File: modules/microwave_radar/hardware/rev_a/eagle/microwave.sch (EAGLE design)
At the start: 55 parts, among them J1 MODULE_GENERIC, J2 TC2030-JLINK-L, U1 SAM4LC8AA, U2 TLV62130, U3 MSGEQ7, U4 HB100

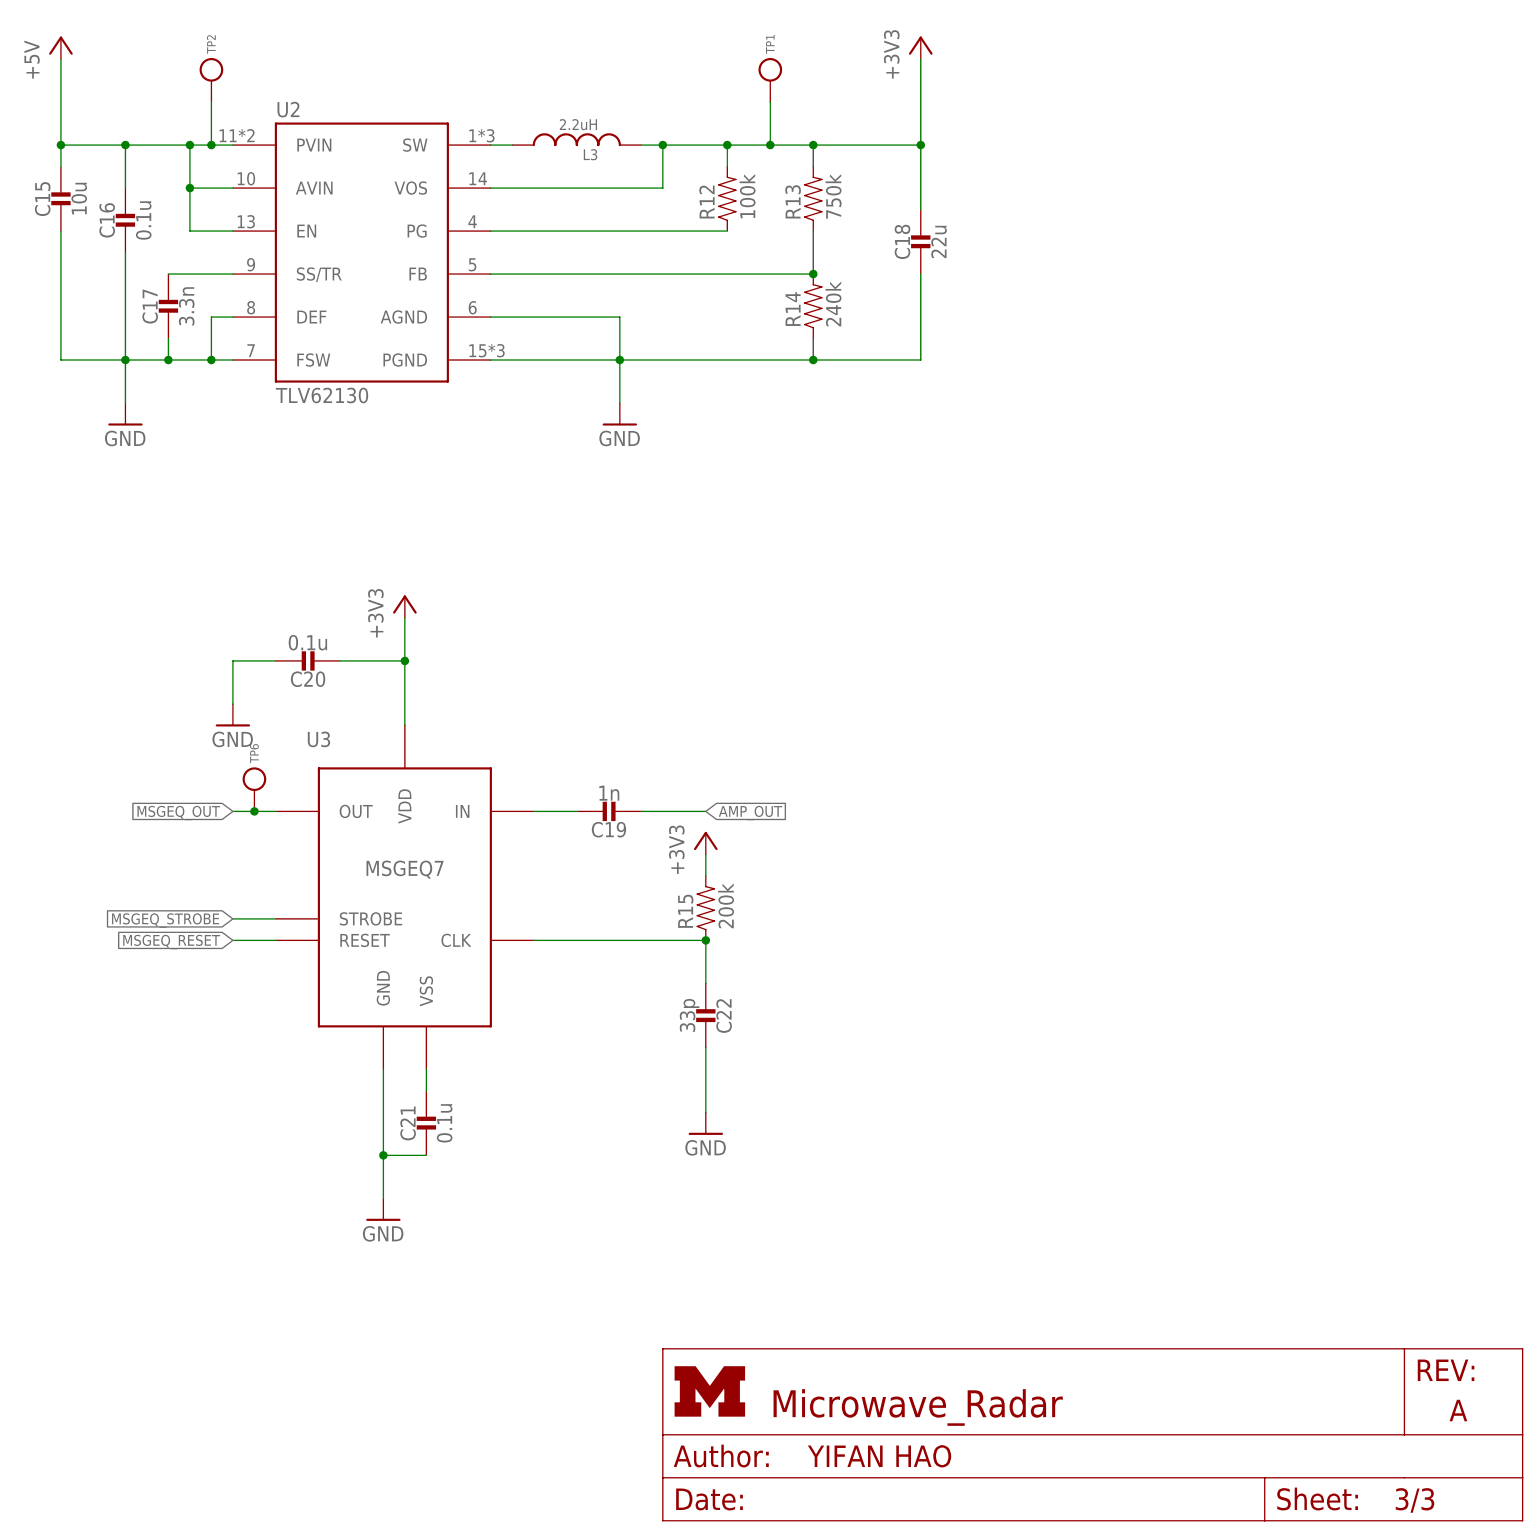
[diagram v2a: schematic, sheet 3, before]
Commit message: Fix test point and trace on the sides
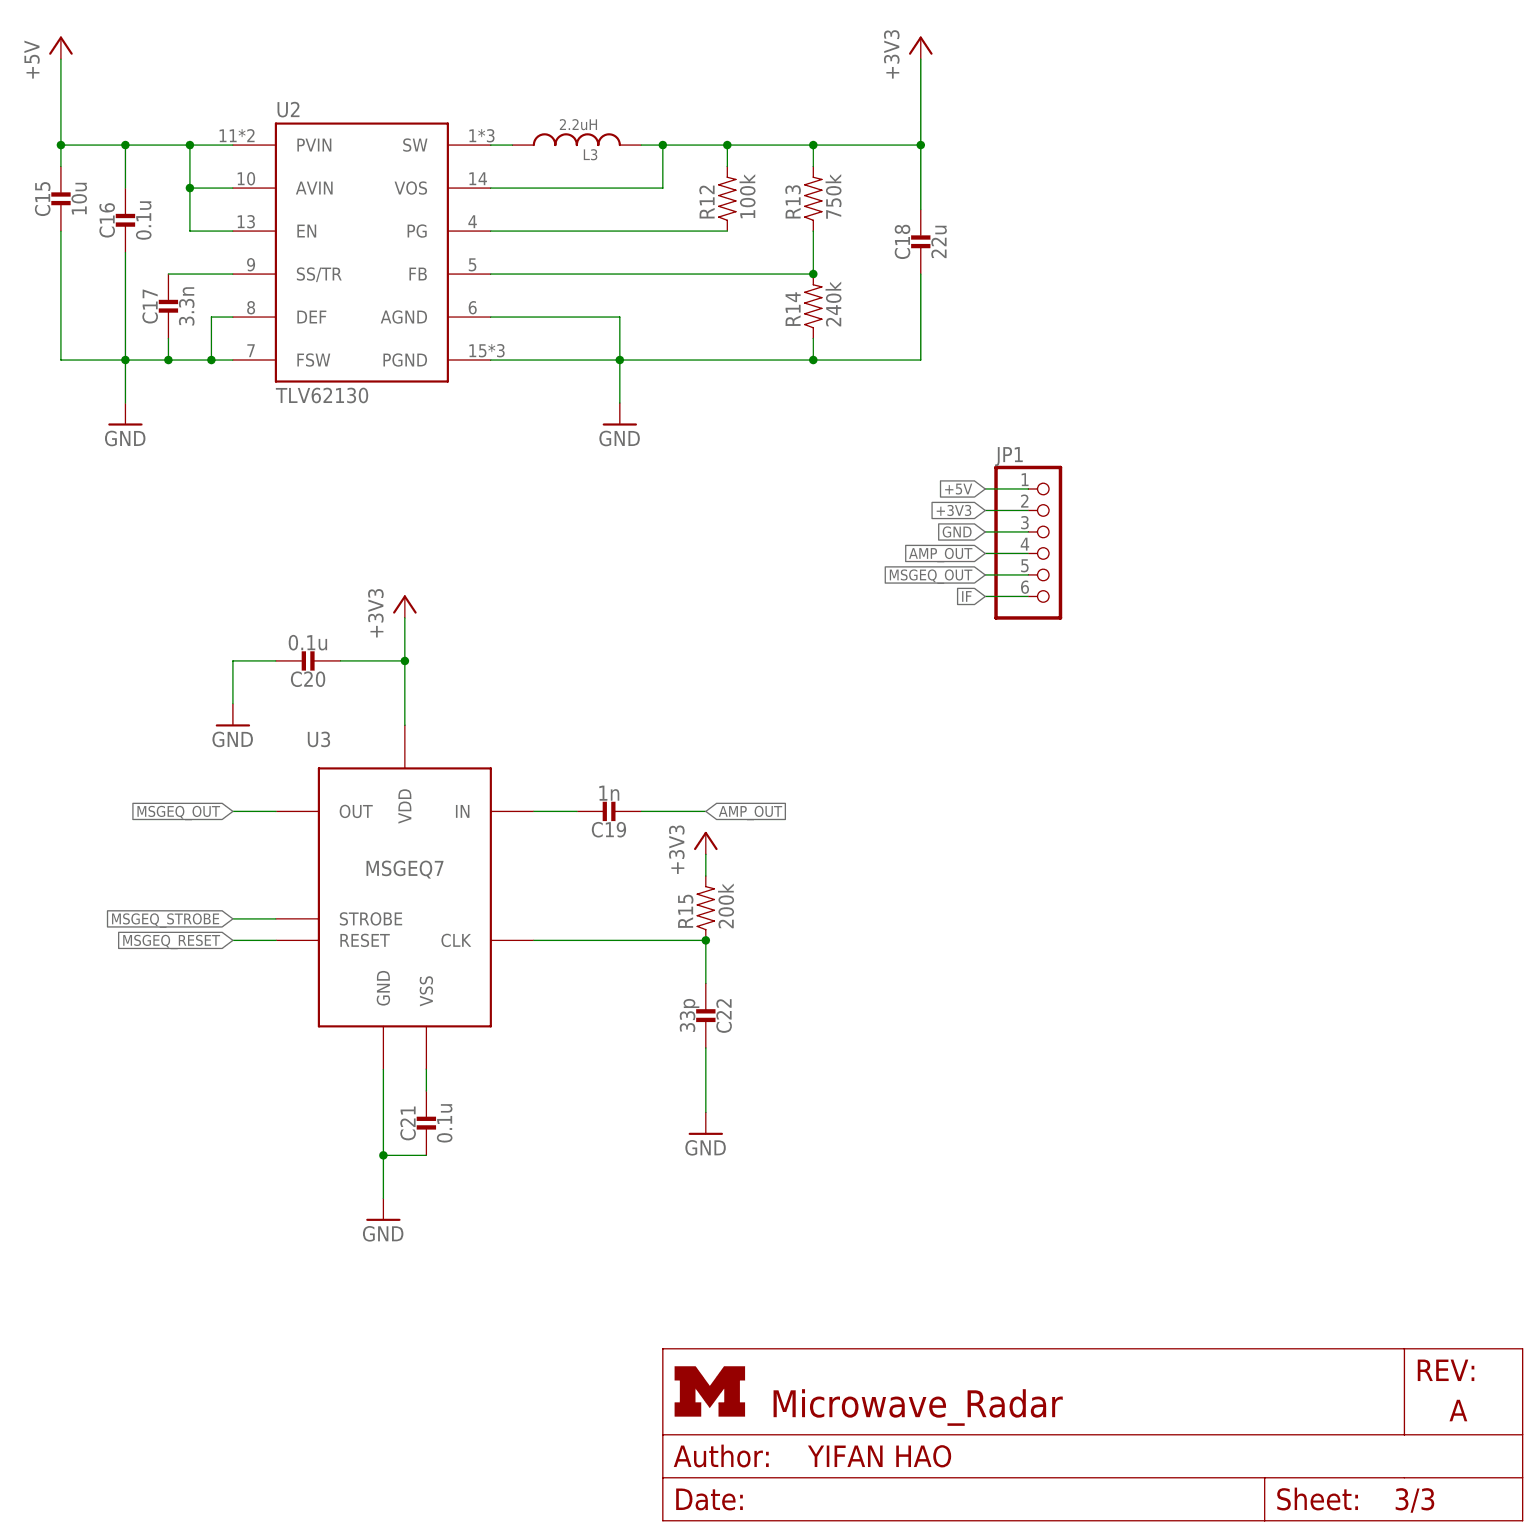
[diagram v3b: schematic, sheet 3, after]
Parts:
- removed TP1, TP2, TP3, TP4, TP5, TP6: TEST_POINT_0.040IN, headers:TEST_POINT_0.040IN
- removed U$1: OP284E_SEPARATE, microwave_radar:OP284E_SEPARATE
- added JP1: (no value), pinhead:PINHD-1X6
- added U5: OP284E_SEPARATE, microwave_radar:OP284E_SEPARATE
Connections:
- net +3V3: now also JP1.2, U5G$2.VCC; no longer TP1.TESTPOINT, U$1G$2.VCC
- net +5V: now also JP1.1; no longer TP2.TESTPOINT
- net AMP_OUT: now also JP1.4, U5_B.OUT_B; no longer TP4.TESTPOINT, U$1G$1.OUT_B
- net GND: now also JP1.3, U5G$2.GND; no longer TP5.TESTPOINT, U$1G$2.GND
- net IF: now also JP1.6; no longer TP3.TESTPOINT
- net MSGEQ_OUT: now also JP1.5; no longer TP6.TESTPOINT
- net N$1: now also U5_B.+IN_B; no longer U$1G$1.+IN_B
- net N$12: now also U5_A.-IN_A; no longer U$1OP284E_A.-IN_A
- net N$17: now also U5_A.OUT_A; no longer U$1OP284E_A.OUT_A
- net N$19: now also U5_B.-IN_B; no longer U$1G$1.-IN_B
- net N$9: now also U5_A.+IN_A; no longer U$1OP284E_A.+IN_A

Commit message: Add attributes for several parts
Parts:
- R3, R4, R5, R8: DIGIKEY (none) -> 1276-3432-1-ND
- R6: DIGIKEY (none) -> 1276-3431-1-ND
- U5: DIGIKEY (none) -> OP284ESZ-ND
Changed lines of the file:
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@@
 <part name="GND1" library="umich" deviceset="GND" device=""/>
 <part name="R2" library="passives" deviceset="RESISTOR" device="0402_RES" value="330k"/>
-<part name="R3" library="passives" deviceset="RESISTOR" device="0402_RES" value="100k"/>
-<part name="R4" library="passives" deviceset="RESISTOR" device="0402_RES" value="100k"/>
+<part name="R3" library="passives" deviceset="RESISTOR" device="0402_RES" value="100k">
+<attribute name="DIGIKEY" value="1276-3432-1-ND"/>
+</part>
+<part name="R4" library="passives" deviceset="RESISTOR" device="0402_RES" value="100k">
+<attribute name="DIGIKEY" value="1276-3432-1-ND"/>
+</part>
 <part name="C2" library="passives" deviceset="CAPACITOR" device="0402_CAP" value="100u"/>
 <part name="GND2" library="umich" deviceset="GND" device=""/>
-<part name="R5" library="passives" deviceset="RESISTOR" device="0402_RES" value="100k"/>
-<part name="R6" library="passives" deviceset="RESISTOR" device="0402_RES" value="10k"/>
+<part name="R5" library="passives" deviceset="RESISTOR" device="0402_RES" value="100k">
+<attribute name="DIGIKEY" value="1276-3432-1-ND"/>
+</part>
+<part name="R6" library="passives" deviceset="RESISTOR" device="0402_RES" value="10k">
+<attribute name="DIGIKEY" value="1276-3431-1-ND"/>
+</part>
 <part name="C3" library="passives" deviceset="CAPACITOR" device="0402_CAP" value="4.7u"/>
 <part name="C4" library="passives" deviceset="CAPACITOR" device="0402_CAP" value="2.2n"/>
@@
 <part name="R7" library="passives" deviceset="RESISTOR" device="0402_RES" value="8.2k"/>
 <part name="C7" library="passives" deviceset="CAPACITOR" device="0402_CAP" value="2.2n"/>
-<part name="R8" library="passives" deviceset="RESISTOR" device="0402_RES" value="100k"/>
+<part name="R8" library="passives" deviceset="RESISTOR" device="0402_RES" value="100k">
+<attribute name="DIGIKEY" value="1276-3432-1-ND"/>
+</part>
 <part name="R11" library="passives" deviceset="RESISTOR" device="0402_RES" value="10k">
 <attribute name="DIGIKEY" value="1276-3431-1-ND"/>
@@
 <part name="GND7" library="umich" deviceset="GND" device=""/>
 <part name="U4" library="microwave_radar" deviceset="HB100" device=""/>
-<part name="U5" library="microwave_radar" deviceset="OP284E_SEPARATE" device=""/>
+<part name="U5" library="microwave_radar" deviceset="OP284E_SEPARATE" device="">
+<attribute name="DIGIKEY" value="OP284ESZ-ND"/>
+</part>
 <part name="JP1" library="pinhead" deviceset="PINHD-1X6" device=""/>
 </parts>
@@
 <instance part="GND1" gate="1" x="17.78" y="25.4"/>
 <instance part="R2" gate="G$1" x="38.1" y="58.42" rot="R90"/>
-<instance part="R3" gate="G$1" x="22.86" y="73.66" rot="R90"/>
-<instance part="R4" gate="G$1" x="22.86" y="91.44" rot="R90"/>
+<instance part="R3" gate="G$1" x="22.86" y="73.66" rot="R90">
+<attribute name="DIGIKEY" x="22.86" y="73.66" size="1.778" layer="96" rot="R90" display="off"/>
+</instance>
+<instance part="R4" gate="G$1" x="22.86" y="91.44" rot="R90">
+<attribute name="DIGIKEY" x="22.86" y="91.44" size="1.778" layer="96" rot="R90" display="off"/>
+</instance>
 <instance part="C2" gate="G$1" x="5.08" y="73.66" rot="R180"/>
 <instance part="GND2" gate="1" x="22.86" y="58.42"/>
-<instance part="R5" gate="G$1" x="45.72" y="10.16" rot="R180"/>
-<instance part="R6" gate="G$1" x="33.02" y="10.16" rot="R180"/>
+<instance part="R5" gate="G$1" x="45.72" y="10.16" rot="R180">
+<attribute name="DIGIKEY" x="45.72" y="10.16" size="1.778" layer="96" rot="R180" display="off"/>
+</instance>
+<instance part="R6" gate="G$1" x="33.02" y="10.16" rot="R180">
+<attribute name="DIGIKEY" x="33.02" y="10.16" size="1.778" layer="96" rot="R180" display="off"/>
+</instance>
 <instance part="C3" gate="G$1" x="20.32" y="10.16" rot="R90"/>
 <instance part="C4" gate="G$1" x="45.72" y="-2.54" rot="R90"/>
@@
 <instance part="R7" gate="G$1" x="104.14" y="43.18" rot="R180"/>
 <instance part="C7" gate="G$1" x="127" y="25.4" rot="R90"/>
-<instance part="R8" gate="G$1" x="127" y="12.7" rot="R180"/>
+<instance part="R8" gate="G$1" x="127" y="12.7" rot="R180">
+<attribute name="DIGIKEY" x="127" y="12.7" size="1.778" layer="96" rot="R180" display="off"/>
+</instance>
 <instance part="GND6" gate="1" x="157.48" y="88.9"/>
 <instance part="+3V1" gate="G$1" x="22.86" y="109.22"/>
@@
 <instance part="GND7" gate="1" x="76.2" y="104.14"/>
 <instance part="U4" gate="G1" x="160.02" y="116.84"/>
-<instance part="U5" gate="_A" x="60.96" y="43.18"/>
+<instance part="U5" gate="_A" x="60.96" y="43.18">
+<attribute name="DIGIKEY" x="60.96" y="43.18" size="1.778" layer="96" display="off"/>
+</instance>
 <instance part="U5" gate="_B" x="119.38" y="45.72"/>
 <instance part="U5" gate="G$2" x="76.2" y="121.92"/>

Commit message: Run Pat's script
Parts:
- C1: value 4.7u -> 8pF; DIGIKEY (none) -> 490-8230-1-ND
- C10, C9: value 100n -> 0.1uF; DIGIKEY 490-10777-1-ND -> (none)
- C11, C12, C14: value 100n -> 100nF
- C13: value 100n -> 100nF; DIGIKEY 490-13252-1-ND -> 490-10777-1-ND
- C15: value 10u -> 100nF; DIGIKEY (none) -> 490-13252-1-ND
- C16: value 0.1u -> 100nF; DIGIKEY (none) -> 490-10777-1-ND
- C17: value 3.3n -> 4.7uF
- C18: value 22u -> 4.7uF
- C19: value 1n -> 4.7uF
- C2: value 100u -> 8pF; DIGIKEY (none) -> 490-8230-1-ND
- C20: value 0.1u -> 10uF
- C21: value 0.1u -> 22uF
- C22: value 33p -> 100uF
- C3: value 4.7u -> 33pF
- C4: value 2.2n -> 1nF
- C5: value 4.7u -> 2.2nF
- C6: value 8pF -> 2.2nF; DIGIKEY 490-8230-1-ND -> (none)
- C7: value 2.2n -> 3.3nF
- C8: value 8pF -> 0.1uF; DIGIKEY 490-8230-1-ND -> (none)
- L1: value 1.5k -> 2.2uH; device passives:FERRITE_BEAD0402 -> passives:INDUCTORIHL; DIGIKEY 490-5216-1-ND -> (none)
- L3: value 2.2uH -> 1.5k; device passives:INDUCTORIHL -> passives:FERRITE_BEAD0402; DIGIKEY (none) -> 490-5216-1-ND
- R1: value 12k -> 8.2k
- R11: value 10k -> 100k; DIGIKEY 1276-3431-1-ND -> (none)
- R12: value 100k -> 200k
- R13: value 750k -> 240k
- R14: value 240k -> 330k
- R15: value 200k -> 750k
- R2: value 330k -> 10k; DIGIKEY (none) -> 1276-3431-1-ND
- R3: value 100k -> 10k; DIGIKEY 1276-3432-1-ND -> 1276-3431-1-ND
- R4: value 100k -> 12k; DIGIKEY 1276-3432-1-ND -> (none)
- R6: value 10k -> 100k; DIGIKEY 1276-3431-1-ND -> 1276-3432-1-ND
- R7: value 8.2k -> 100k; DIGIKEY (none) -> 1276-3432-1-ND
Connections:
- net +3V3: now also C12.2, C13.2, C21.1, L1.2, L3.P$2, R3.2, R5.2, R6.2, R8.2; no longer C10.2, C18.1, C20.2, L1.P$2, L3.2, R10.2, R13.2, R4.2, R9.2
- net +5V: now also C20.1, C8.1; no longer C15.1, C16.1
- net AMP_OUT: now also C4.2, C6.2, R10.1; no longer C19.2, C7.2, R8.1
- net CONTROLLER_SWDCLK: now also R6.1; no longer R10.1
- net CONTROLLER_SWDIO: now also R5.1; no longer R9.1
- net CONTROLLER_XIN: now also C1.1; no longer C6.1
- net CONTROLLER_XOUT: now also C2.1; no longer C8.1
- net GND: now also C1.2, C10.2, C15.1, C16.1, C18.1, C2.2, C20.2, C7.2, R13.1, R4.1, R7.1; no longer C10.1, C15.2, C16.2, C17.2, C18.2, C2.1, C20.1, C6.2, R1.1, R14.1, R3.1
- net IF: now also C17.1, R4.2; no longer C1.1, R1.2
- net N$1: now also C22.2, R14.2, R7.2, R8.1; no longer C2.2, R2.2, R3.2, R4.1
- net N$12: now also C5.1, R2.1, R9.2; no longer C4.1, R5.2, R6.1
- net N$13: now also C14.2, L3.P$1; no longer C12.2, L1.P$1
- net N$14: now also R3.1; no longer R11.1
- net N$15: now also C18.2, R2.2; no longer C3.2, R6.2
- net N$17: now also C19.1, C5.2, R9.1; no longer C4.2, C5.1, R5.1
- net N$18: now also C19.2, R1.2; no longer C5.2, R7.2
- net N$19: now also C6.1, R1.1, R10.2; no longer C7.1, R7.1, R8.2
- net N$2: now also C3.2, R12.1; no longer C22.2, R15.1
- net N$20: now also L1.1; no longer L3.1
- net N$23: now also R11.1; no longer R12.1
- net N$24: now also R13.2, R15.1; no longer R13.1, R14.2
- net N$3: now also C4.1; no longer C19.1
- net N$6: now also C15.2, C16.2; no longer C13.2, C14.2
- net N$7: now also C10.1; no longer C21.1
- net N$8: now also C7.1; no longer C17.1
- net N$9: now also C17.2, R14.1; no longer C1.2, R2.1
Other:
- moved on the sheet: C11, C12, C13, C14, C20, C21, C5, R1, R12, R13, R15, R2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

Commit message: Finish adding attribute
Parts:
- removed C10, C9: 0.1uF, passives:CAPACITOR0402_CAP
- removed C4: 1nF, passives:CAPACITOR0402_CAP
- removed R12: 200k, passives:RESISTOR0402_RES
- added C23: 10uF, passives:CAPACITOR0805_CAP
- added C24: 0.1uF, passives:CAPACITOR0603_CAP
- added C25: 33pF, passives:CAPACITOR0603_CAP
- added R16: 200k, passives:RESISTOR0603_RES
- C17, C18, C19: DIGIKEY (none) -> 1276-1481-1-ND
- C20: value 10uF -> 22uF; device passives:CAPACITOR0402_CAP -> passives:CAPACITOR0603_CAP; DIGIKEY (none) -> 1276-1193-1-ND
- C21: value 22uF -> 0.1uF; device passives:CAPACITOR0402_CAP -> passives:CAPACITOR0603_CAP; DIGIKEY (none) -> 490-1532-1-ND
- C22: device passives:CAPACITOR0402_CAP -> passives:CAPACITOR1210_CAP; DIGIKEY (none) -> 490-3390-1-ND
- C3: value 33pF -> 1nF; device passives:CAPACITOR0402_CAP -> passives:CAPACITOR0603_CAP; DIGIKEY (none) -> 490-1494-1-ND
- C5, C6: DIGIKEY (none) -> 490-11418-1-ND
- C7: DIGIKEY (none) -> 490-3248-1-ND
- C8: DIGIKEY (none) -> 490-5920-1-ND
- R1: DIGIKEY (none) -> 311-8.20KLRCT-ND
- R11: DGIKEY (none) -> P100KJCT-ND
- R13: DIGIKEY (none) -> P240KLCT-ND
- R14: DIGIKEY (none) -> 1276-4244-1-ND
- R15: DIGIKEY (none) -> P750KLCT-ND
- R4: DIGIKEY (none) -> 1276-4122-1-ND
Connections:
- net +3V3: now also C20.1, C21.2, R16.1; no longer C21.1, C9.2, R12.2
- net +5V: now also C23.1; no longer C20.1
- net AMP_OUT: now also C3.2; no longer C4.2
- net GND: now also C21.1, C23.2, C24.2, C25.2; no longer C10.2, C21.2, C3.1, C9.1
- net N$2: now also C25.1, R16.2; no longer C3.2, R12.1
- net N$3: now also C3.1; no longer C4.1
- net N$7: now also C24.1; no longer C10.1
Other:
- moved on the sheet: C20, C21, C3
